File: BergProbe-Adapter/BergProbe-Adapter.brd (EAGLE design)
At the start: 92.7 x 29.8 mm, 8 parts, among them U1 TSR_1-24_

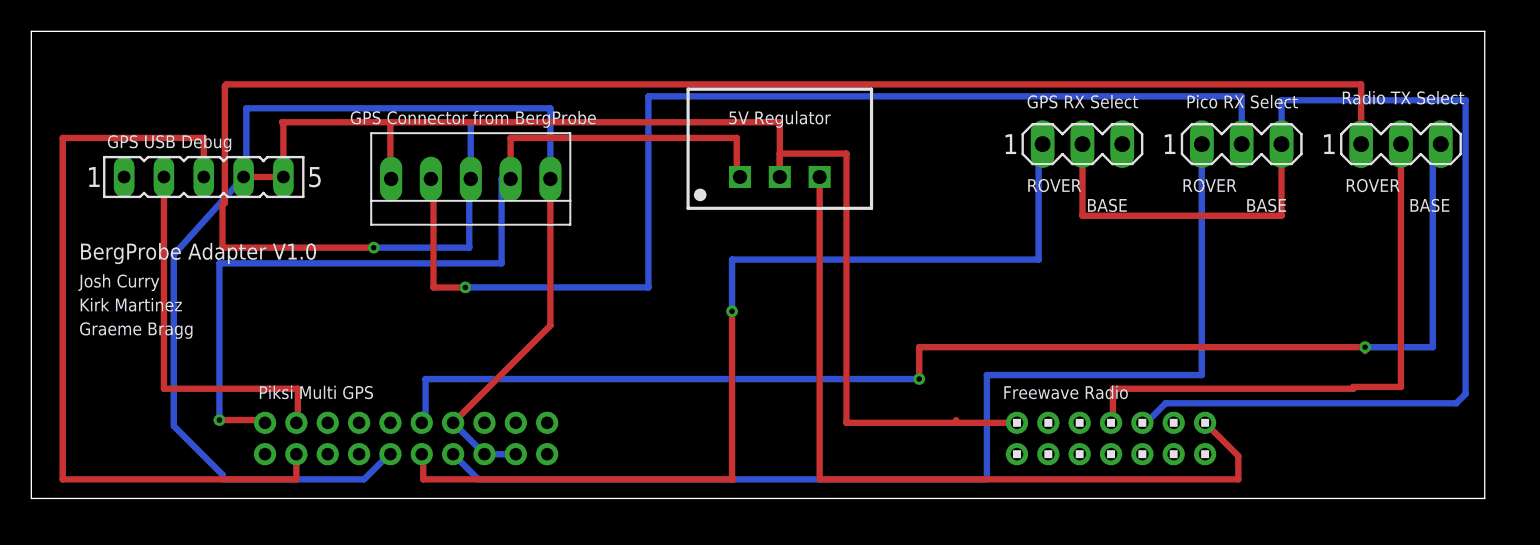
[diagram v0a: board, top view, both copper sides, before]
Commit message: Added mounting holes. Will need checking; only done roughly with callipers.
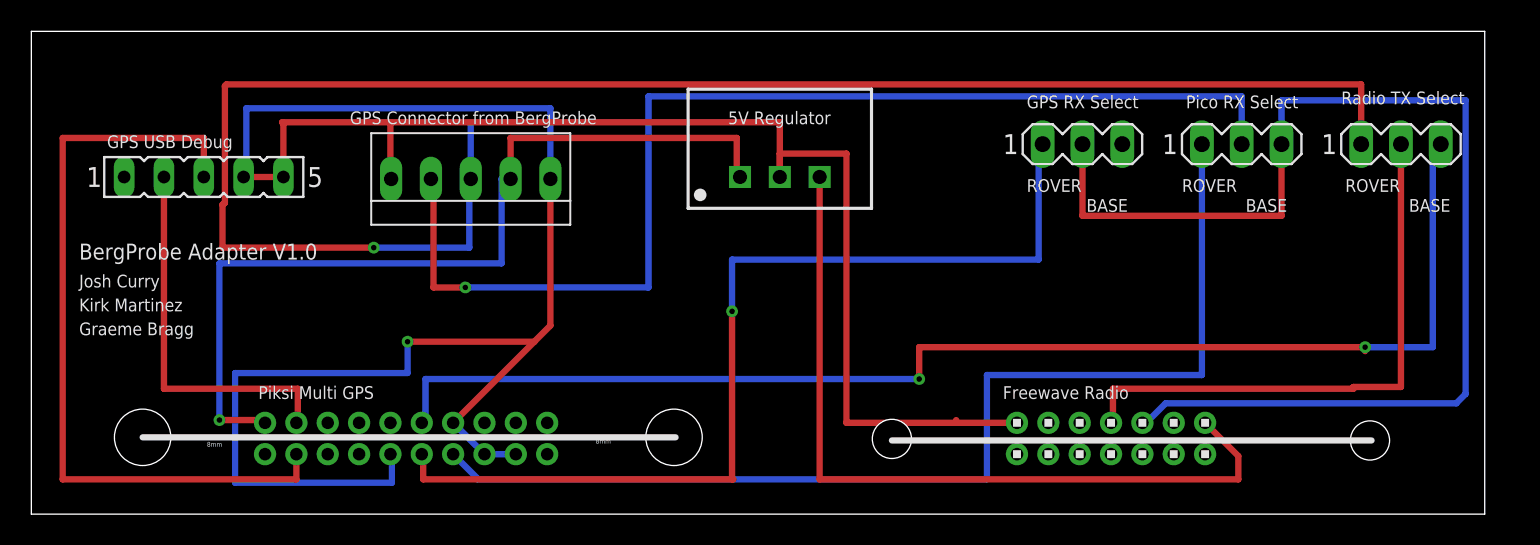
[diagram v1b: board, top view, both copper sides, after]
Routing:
- net GND: track 164.9 -> 171.3 mm, vias 0 -> 1
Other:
- board size 92.7 x 29.8 mm -> 92.7 x 30.8 mm
- board text added: "8mm"
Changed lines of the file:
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@@
 <setting verticaltext="up"/>
 </settings>
-<grid distance="10" unitdist="mil" unit="mil" style="lines" multiple="1" display="no" altdistance="1" altunitdist="mil" altunit="mil"/>
+<grid distance="0.1" unitdist="mm" unit="mm" style="lines" multiple="1" display="no" altdistance="1" altunitdist="mm" altunit="mm"/>
 <layers>
 <layer number="1" name="Top" color="4" fill="1" visible="yes" active="yes"/>
@@
 <layer number="27" name="tValues" color="7" fill="1" visible="yes" active="yes"/>
 <layer number="28" name="bValues" color="7" fill="1" visible="yes" active="yes"/>
-<layer number="29" name="tStop" color="7" fill="3" visible="no" active="yes"/>
-<layer number="30" name="bStop" color="7" fill="6" visible="no" active="yes"/>
-<layer number="31" name="tCream" color="7" fill="4" visible="no" active="yes"/>
-<layer number="32" name="bCream" color="7" fill="5" visible="no" active="yes"/>
-<layer number="33" name="tFinish" color="6" fill="3" visible="no" active="yes"/>
-<layer number="34" name="bFinish" color="6" fill="6" visible="no" active="yes"/>
-<layer number="35" name="tGlue" color="7" fill="4" visible="no" active="yes"/>
-<layer number="36" name="bGlue" color="7" fill="5" visible="no" active="yes"/>
-<layer number="37" name="tTest" color="7" fill="1" visible="no" active="yes"/>
-<layer number="38" name="bTest" color="7" fill="1" visible="no" active="yes"/>
+<layer number="29" name="tStop" color="7" fill="3" visible="yes" active="yes"/>
+<layer number="30" name="bStop" color="7" fill="6" visible="yes" active="yes"/>
+<layer number="31" name="tCream" color="7" fill="4" visible="yes" active="yes"/>
+<layer number="32" name="bCream" color="7" fill="5" visible="yes" active="yes"/>
+<layer number="33" name="tFinish" color="6" fill="3" visible="yes" active="yes"/>
+<layer number="34" name="bFinish" color="6" fill="6" visible="yes" active="yes"/>
+<layer number="35" name="tGlue" color="7" fill="4" visible="yes" active="yes"/>
+<layer number="36" name="bGlue" color="7" fill="5" visible="yes" active="yes"/>
+<layer number="37" name="tTest" color="7" fill="1" visible="yes" active="yes"/>
+<layer number="38" name="bTest" color="7" fill="1" visible="yes" active="yes"/>
 <layer number="39" name="tKeepout" color="4" fill="11" visible="yes" active="yes"/>
 <layer number="40" name="bKeepout" color="1" fill="11" visible="yes" active="yes"/>
@@
 <layer number="42" name="bRestrict" color="1" fill="10" visible="yes" active="yes"/>
 <layer number="43" name="vRestrict" color="2" fill="10" visible="yes" active="yes"/>
-<layer number="44" name="Drills" color="7" fill="1" visible="no" active="yes"/>
-<layer number="45" name="Holes" color="7" fill="1" visible="no" active="yes"/>
-<layer number="46" name="Milling" color="3" fill="1" visible="no" active="yes"/>
-<layer number="47" name="Measures" color="7" fill="1" visible="no" active="yes"/>
+<layer number="44" name="Drills" color="7" fill="1" visible="yes" active="yes"/>
+<layer number="45" name="Holes" color="7" fill="1" visible="yes" active="yes"/>
+<layer number="46" name="Milling" color="3" fill="1" visible="yes" active="yes"/>
+<layer number="47" name="Measures" color="7" fill="1" visible="yes" active="yes"/>
 <layer number="48" name="Document" color="7" fill="1" visible="yes" active="yes"/>
 <layer number="49" name="Reference" color="7" fill="1" visible="yes" active="yes"/>
@@
 <board>
 <plain>
-<wire x1="0" y1="0" x2="92.72" y2="0" width="0" layer="20"/>
-<wire x1="92.72" y1="0" x2="92.72" y2="29.8" width="0" layer="20"/>
+<wire x1="0" y1="-1" x2="92.72" y2="-1" width="0" layer="20"/>
+<wire x1="92.72" y1="-1" x2="92.72" y2="29.8" width="0" layer="20"/>
 <wire x1="92.72" y1="29.8" x2="0" y2="29.8" width="0" layer="20"/>
-<wire x1="0" y1="29.8" x2="0" y2="0" width="0" layer="20"/>
+<wire x1="0" y1="29.8" x2="0" y2="-1" width="0" layer="20"/>
 <text x="3.048" y="15.24" size="1.016" layer="25">BergProbe Adapter V1.0</text>
 <text x="3.048" y="13.462" size="0.8128" layer="25">Josh Curry</text>
@@
 <text x="14.478" y="6.35" size="0.8128" layer="25">Piksi Multi GPS</text>
 <text x="61.976" y="6.35" size="0.8128" layer="25">Freewave Radio</text>
+<hole x="41" y="3.9" drill="3.6"/>
+<hole x="7.1" y="3.9" drill="3.6"/>
+<text x="11.2" y="3.3" size="0.3048" layer="25">8mm</text>
+<text x="36" y="3.5" size="0.3048" layer="25">8mm</text>
+<hole x="54.9" y="3.8" drill="2.5"/>
+<hole x="85.4" y="3.7" drill="2.5"/>
+<wire x1="85.5" y1="3.7" x2="54.9" y2="3.7" width="0.4" layer="25"/>
+<wire x1="7.1" y1="3.9" x2="41.1" y2="3.9" width="0.4" layer="25"/>
 </plain>
 <attributes>
@@
 <wire x1="16" y1="24" x2="22.908734375" y2="24" width="0.4064" layer="1"/>
 <wire x1="22.826" y1="2.826" x2="22.908" y2="2.826" width="0.4064" layer="16"/>
-<wire x1="22.826" y1="2.826" x2="21.2192" y2="1.2192" width="0.4064" layer="16"/>
-<wire x1="21.2192" y1="1.2192" x2="12.2192" y2="1.2192" width="0.4064" layer="16"/>
-<wire x1="9.0884" y1="4.6224" x2="9.0884" y2="15.5484" width="0.4064" layer="16"/>
-<wire x1="9.0884" y1="15.5484" x2="13.54" y2="20.508" width="0.4064" layer="16"/>
-<wire x1="12.2192" y1="1.2192" x2="12.2192" y2="1.4916" width="0.4064" layer="16"/>
-<wire x1="12.2192" y1="1.4916" x2="9.0884" y2="4.6224" width="0.4064" layer="16"/>
 <wire x1="28.908" y1="2.826" x2="30.908" y2="2.826" width="0.4064" layer="16"/>
-<wire x1="26.908" y1="4.826" x2="28.908" y2="2.826" width="0.4064" layer="16"/>
+<wire x1="28.908" y1="2.826" x2="26.908" y2="4.826" width="0.4064" layer="16"/>
 <wire x1="62.88" y1="4.826" x2="59" y2="4.826" width="0.4064" layer="1"/>
 <wire x1="59" y1="4.826" x2="59" y2="5" width="0.4064" layer="1"/>
@@
 <wire x1="22.908734375" y1="24" x2="47.75" y2="24" width="0.4064" layer="1"/>
 <wire x1="47.75" y1="24" x2="47.75" y2="20.51" width="0.4064" layer="1"/>
-<wire x1="26.908" y1="4.826" x2="33.113" y2="11.031" width="0.4064" layer="1"/>
+<wire x1="32.10076875" y1="10.01876875" x2="26.908" y2="4.826" width="0.4064" layer="1"/>
+<wire x1="32.10076875" y1="10.01876875" x2="33.113" y2="11.031" width="0.4064" layer="1"/>
 <wire x1="33.113" y1="11.031" x2="33.113" y2="20.383" width="0.4064" layer="1"/>
+<wire x1="22.908" y1="2.826" x2="23" y2="2.826" width="0.4" layer="16"/>
+<wire x1="23" y1="2.826" x2="23" y2="1" width="0.4" layer="16"/>
+<wire x1="23" y1="1" x2="13" y2="1" width="0.4" layer="16"/>
+<wire x1="13" y1="1" x2="13" y2="8" width="0.4" layer="16"/>
+<wire x1="13" y1="8" x2="24" y2="8" width="0.4" layer="16"/>
+<wire x1="24" y1="8" x2="24" y2="10" width="0.4" layer="16"/>
+<via x="24" y="10" extent="1-16" drill="0.35"/>
+<wire x1="24" y1="10" x2="32.10076875" y2="10" width="0.4" layer="1"/>
+<wire x1="32.10076875" y1="10" x2="32.10076875" y2="10.01876875" width="0.4" layer="1"/>
 </signal>
 <signal name="PICO_TX">

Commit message: Modified hole placings. Also moved tracks away from holes just in case.
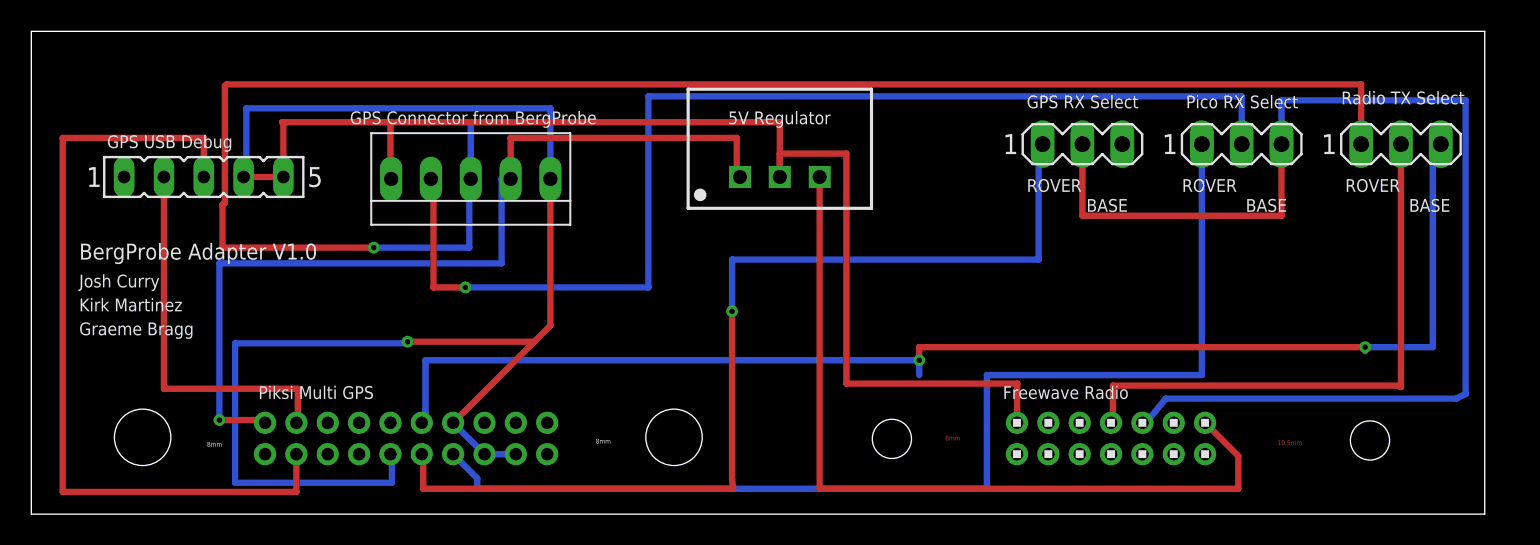
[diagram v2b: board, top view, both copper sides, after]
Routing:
- net GPS_USB0+: track 49.8 -> 51.4 mm
- net GPS_UART1_TX: track 69.9 -> 71.1 mm
- net 5V: track 50.5 -> 51.7 mm
- net GPS_UART0_RX: track 62.7 -> 63.8 mm
- net GPS_UART0_TX: track 83.3 -> 84.0 mm
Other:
- board text added: "10.5mm"
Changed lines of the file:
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@@
 <hole x="54.9" y="3.8" drill="2.5"/>
 <hole x="85.4" y="3.7" drill="2.5"/>
-<wire x1="85.5" y1="3.7" x2="54.9" y2="3.7" width="0.4" layer="25"/>
-<wire x1="7.1" y1="3.9" x2="41.1" y2="3.9" width="0.4" layer="25"/>
+<text x="79.5" y="3.4" size="0.3048" layer="1">10.5mm</text>
+<text x="58.3" y="3.7" size="0.3048" layer="1">8mm</text>
 </plain>
 <attributes>
@@
 <wire x1="28.908" y1="2.826" x2="30.908" y2="2.826" width="0.4064" layer="16"/>
 <wire x1="28.908" y1="2.826" x2="26.908" y2="4.826" width="0.4064" layer="16"/>
-<wire x1="62.88" y1="4.826" x2="59" y2="4.826" width="0.4064" layer="1"/>
-<wire x1="59" y1="4.826" x2="59" y2="5" width="0.4064" layer="1"/>
-<wire x1="59" y1="4.826" x2="52" y2="4.826" width="0.4064" layer="1"/>
-<wire x1="52" y1="4.826" x2="52" y2="22" width="0.4064" layer="1"/>
+<wire x1="62.88" y1="4.826" x2="62.9" y2="7.326" width="0.4064" layer="1"/>
+<wire x1="62.9" y1="7.326" x2="52" y2="7.326" width="0.4064" layer="1"/>
+<wire x1="52" y1="7.326" x2="52" y2="22" width="0.4064" layer="1"/>
 <wire x1="52" y1="22" x2="47.75" y2="22" width="0.4064" layer="1"/>
 <wire x1="47.75" y1="20.51" x2="47.75" y2="22" width="0.4064" layer="1"/>
@@
 <wire x1="23" y1="2.826" x2="23" y2="1" width="0.4" layer="16"/>
 <wire x1="23" y1="1" x2="13" y2="1" width="0.4" layer="16"/>
-<wire x1="13" y1="1" x2="13" y2="8" width="0.4" layer="16"/>
-<wire x1="13" y1="8" x2="24" y2="8" width="0.4" layer="16"/>
-<wire x1="24" y1="8" x2="24" y2="10" width="0.4" layer="16"/>
+<wire x1="13" y1="1" x2="13" y2="9.9" width="0.4" layer="16"/>
+<wire x1="13" y1="9.9" x2="24" y2="9.9" width="0.4" layer="16"/>
+<wire x1="24" y1="9.9" x2="24" y2="10" width="0.4" layer="16"/>
 <via x="24" y="10" extent="1-16" drill="0.35"/>
 <wire x1="24" y1="10" x2="32.10076875" y2="10" width="0.4" layer="1"/>
@@
 <contactref element="GPS" pad="4"/>
 <contactref element="USB" pad="3"/>
-<wire x1="16.908" y1="2.826" x2="16.908" y2="1.2192" width="0.4064" layer="1"/>
-<wire x1="16.908" y1="1.2192" x2="2" y2="1.2192" width="0.4064" layer="1"/>
-<wire x1="2" y1="1.2192" x2="2" y2="23" width="0.4064" layer="1"/>
+<wire x1="16.908" y1="2.826" x2="16.908" y2="0.4192" width="0.4064" layer="1"/>
+<wire x1="16.908" y1="0.4192" x2="2" y2="0.4192" width="0.4064" layer="1"/>
+<wire x1="2" y1="0.4192" x2="2" y2="23" width="0.4064" layer="1"/>
 <wire x1="2" y1="23" x2="11" y2="23" width="0.4064" layer="1"/>
 <wire x1="11" y1="23" x2="11" y2="20.508" width="0.4064" layer="1"/>
@@
 <wire x1="89.916" y1="22.606" x2="89.408" y2="22.606" width="0.4064" layer="16"/>
 <wire x1="89.408" y1="9.652" x2="89.408" y2="22.606" width="0.4064" layer="16"/>
-<wire x1="89.408" y1="9.961075" x2="89.408" y2="8.128" width="0" layer="19" extent="1-16"/>
 <wire x1="24.908" y1="4.826" x2="25.146" y2="4.826" width="0.4064" layer="16"/>
-<wire x1="25.146" y1="4.826" x2="25.146" y2="7.62" width="0.4064" layer="16"/>
-<wire x1="25.146" y1="7.62" x2="56.642" y2="7.62" width="0.4064" layer="16"/>
-<wire x1="56.642" y1="7.874" x2="56.642" y2="7.62" width="0.4064" layer="16"/>
-<via x="56.642" y="7.62" extent="1-16" drill="0.35"/>
-<wire x1="56.642" y1="7.62" x2="56.642" y2="9.652" width="0.4064" layer="1"/>
+<wire x1="25.146" y1="4.826" x2="25.146" y2="8.82" width="0.4064" layer="16"/>
+<wire x1="25.146" y1="8.82" x2="56.642" y2="8.82" width="0.4064" layer="16"/>
+<wire x1="56.642" y1="7.874" x2="56.642" y2="8.82" width="0.4064" layer="16"/>
+<via x="56.642" y="8.82" extent="1-16" drill="0.35"/>
+<wire x1="56.642" y1="8.82" x2="56.642" y2="9.652" width="0.4064" layer="1"/>
 <wire x1="56.642" y1="9.652" x2="85.09" y2="9.652" width="0.4064" layer="1"/>
 <wire x1="85.09" y1="9.398" x2="85.09" y2="9.652" width="0.4064" layer="1"/>
 <via x="85.09" y="9.652" extent="1-16" drill="0.35"/>
 <wire x1="85.09" y1="9.652" x2="89.408" y2="9.652" width="0.4064" layer="16"/>
-<wire x1="89.408" y1="9.652" x2="89.408" y2="9.961075" width="0" layer="19" extent="1-16"/>
 </signal>
 <signal name="GPS_UART0_RX">
@@
 <contactref element="GPSRXSEL" pad="1"/>
 <wire x1="24.908" y1="2.826" x2="25" y2="2.734" width="0.4064" layer="1"/>
-<wire x1="25" y1="2.734" x2="25" y2="1.2192" width="0.4064" layer="1"/>
-<wire x1="25" y1="1.2192" x2="44.778" y2="1.2192" width="0.4064" layer="1"/>
+<wire x1="25" y1="2.734" x2="25" y2="0.6192" width="0.4064" layer="1"/>
+<wire x1="25" y1="0.6192" x2="44.778" y2="0.6192" width="0.4064" layer="1"/>
 <wire x1="64.516" y1="22.606" x2="64.262" y2="22.606" width="0.4064" layer="16"/>
 <wire x1="64.262" y1="22.606" x2="64.262" y2="15.24" width="0.4064" layer="16"/>
@@
 <wire x1="44.704" y1="15.24" x2="44.704" y2="11.938" width="0.4064" layer="16"/>
 <via x="44.704" y="11.938" extent="1-16" drill="0.35"/>
-<wire x1="44.778" y1="1.2192" x2="44.704" y2="1.2192" width="0.4064" layer="1"/>
+<wire x1="44.778" y1="0.6192" x2="44.704" y2="1.2192" width="0.4064" layer="1"/>
 <wire x1="44.704" y1="1.2192" x2="44.704" y2="11.938" width="0.4064" layer="1"/>
 </signal>
@@
 <contactref element="RXSEL" pad="1"/>
 <wire x1="26.908" y1="2.826" x2="28.448" y2="1.286" width="0.4064" layer="16"/>
-<wire x1="28.448" y1="1.286" x2="28.448" y2="1.2192" width="0.4064" layer="16"/>
-<wire x1="28.448" y1="1.2192" x2="60.96" y2="1.2192" width="0.4064" layer="16"/>
-<wire x1="60.96" y1="1.2192" x2="60.96" y2="7.874" width="0.4064" layer="16"/>
+<wire x1="28.448" y1="1.286" x2="28.448" y2="0.6192" width="0.4064" layer="16"/>
+<wire x1="28.448" y1="0.6192" x2="60.96" y2="0.6192" width="0.4064" layer="16"/>
+<wire x1="60.96" y1="0.6192" x2="60.96" y2="7.874" width="0.4064" layer="16"/>
 <wire x1="60.96" y1="7.874" x2="74.676" y2="7.874" width="0.4064" layer="16"/>
 <wire x1="74.676" y1="7.874" x2="74.676" y2="22.606" width="0.4064" layer="16"/>
@@
 <contactref element="U1" pad="3"/>
 <wire x1="74.88" y1="4.826" x2="77" y2="2.706" width="0.4064" layer="1"/>
-<wire x1="77" y1="2.706" x2="77" y2="1.2192" width="0.4064" layer="1"/>
-<wire x1="77" y1="1.2192" x2="50.29" y2="1.2192" width="0.4064" layer="1"/>
-<wire x1="50.29" y1="1.2192" x2="50.29" y2="20.51" width="0.4064" layer="1"/>
+<wire x1="77" y1="2.706" x2="77" y2="0.6192" width="0.4064" layer="1"/>
+<wire x1="77" y1="0.6192" x2="50.29" y2="0.6192" width="0.4064" layer="1"/>
+<wire x1="50.29" y1="0.6192" x2="50.29" y2="20.51" width="0.4064" layer="1"/>
 </signal>
 <signal name="RADIO_TXD">
@@
 <contactref element="GPSRXSEL" pad="2"/>
 <wire x1="70.88" y1="4.826" x2="71.11986875" y2="4.826" width="0.4064" layer="16"/>
-<wire x1="71.11986875" y1="4.826" x2="72.36446875" y2="6.0706" width="0.4064" layer="16"/>
-<wire x1="72.36446875" y1="6.0706" x2="90.9066" y2="6.0706" width="0.4064" layer="16"/>
+<wire x1="71.11986875" y1="4.826" x2="72.36446875" y2="6.3706" width="0.4064" layer="16"/>
+<wire x1="72.36446875" y1="6.3706" x2="90.9066" y2="6.3706" width="0.4064" layer="16"/>
 <wire x1="91.5008" y1="6.6648" x2="91.5008" y2="25.4" width="0.4064" layer="16"/>
 <wire x1="91.5008" y1="25.4" x2="79.756" y2="25.4" width="0.4064" layer="16"/>
 <wire x1="79.756" y1="25.4" x2="79.756" y2="22.606" width="0.4064" layer="16"/>
-<wire x1="90.9066" y1="6.0706" x2="91.5008" y2="6.6648" width="0.4064" layer="16"/>
+<wire x1="90.9066" y1="6.3706" x2="91.5008" y2="6.6648" width="0.4064" layer="16"/>
 <wire x1="79.756" y1="22.606" x2="79.756" y2="18.034" width="0.4064" layer="1"/>
 <wire x1="79.756" y1="18.034" x2="67.056" y2="18.034" width="0.4064" layer="1"/>
@@
 <contactref element="TXSEL" pad="2"/>
 <wire x1="68.88" y1="4.826" x2="69" y2="4.826" width="0.4064" layer="1"/>
-<wire x1="69" y1="4.826" x2="69" y2="7" width="0.4064" layer="1"/>
-<wire x1="84.342" y1="7" x2="69" y2="7" width="0.4064" layer="1"/>
+<wire x1="69" y1="4.826" x2="69" y2="7.2" width="0.4064" layer="1"/>
+<wire x1="87.342" y1="7.2" x2="69" y2="7.2" width="0.4064" layer="1"/>
 <wire x1="87.376" y1="22.606" x2="87.376" y2="7.112" width="0.4064" layer="1"/>
-<wire x1="87.376" y1="7.112" x2="84.342" y2="7.112" width="0.4064" layer="1"/>
-<wire x1="84.342" y1="7.112" x2="84.342" y2="7" width="0.4064" layer="1"/>
+<wire x1="87.376" y1="7.112" x2="87.342" y2="7.112" width="0.4064" layer="1"/>
+<wire x1="87.342" y1="7.112" x2="87.342" y2="7.2" width="0.4064" layer="1"/>
 </signal>
 <signal name="PICO_RX">
